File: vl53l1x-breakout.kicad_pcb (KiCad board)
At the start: 4 copper layers, 28 x 21.5 mm, 30 parts, among them J0 SM07B-SRSS-TBLFSN, J1 SM07B-SRSS-TBLFSN, U1 PCA9615DPJ, U2 VL53L1CXV0FY_1, U3 LTC4316IMSPBF

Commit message: cleanup routing a bit
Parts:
- moved C1 6.17 mm to (115.9, 132.3), turned to 0 degrees
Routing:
- net VCC: track 40.8 -> 53.0 mm, vias 9 -> 10
- net shld: track 32.3 -> 29.5 mm
- net GND: track 30.3 -> 31.4 mm
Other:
- board text added: "VL53L1X diff. breakout @kemfic 2022 rev. 0"
- board text removed: "VL53L1X Diff. Breakout @kemfic 2022 rev. 0"

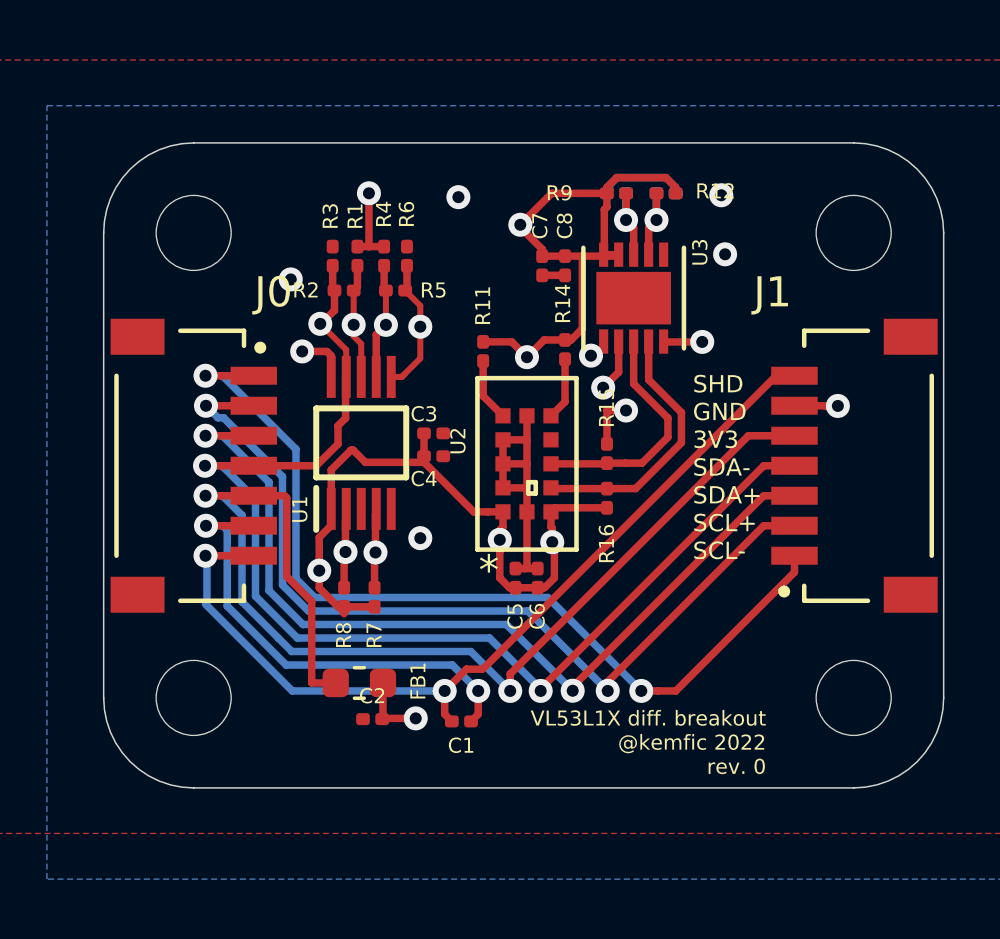
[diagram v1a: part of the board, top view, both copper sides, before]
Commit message: ordered but the pinout is flipped :/
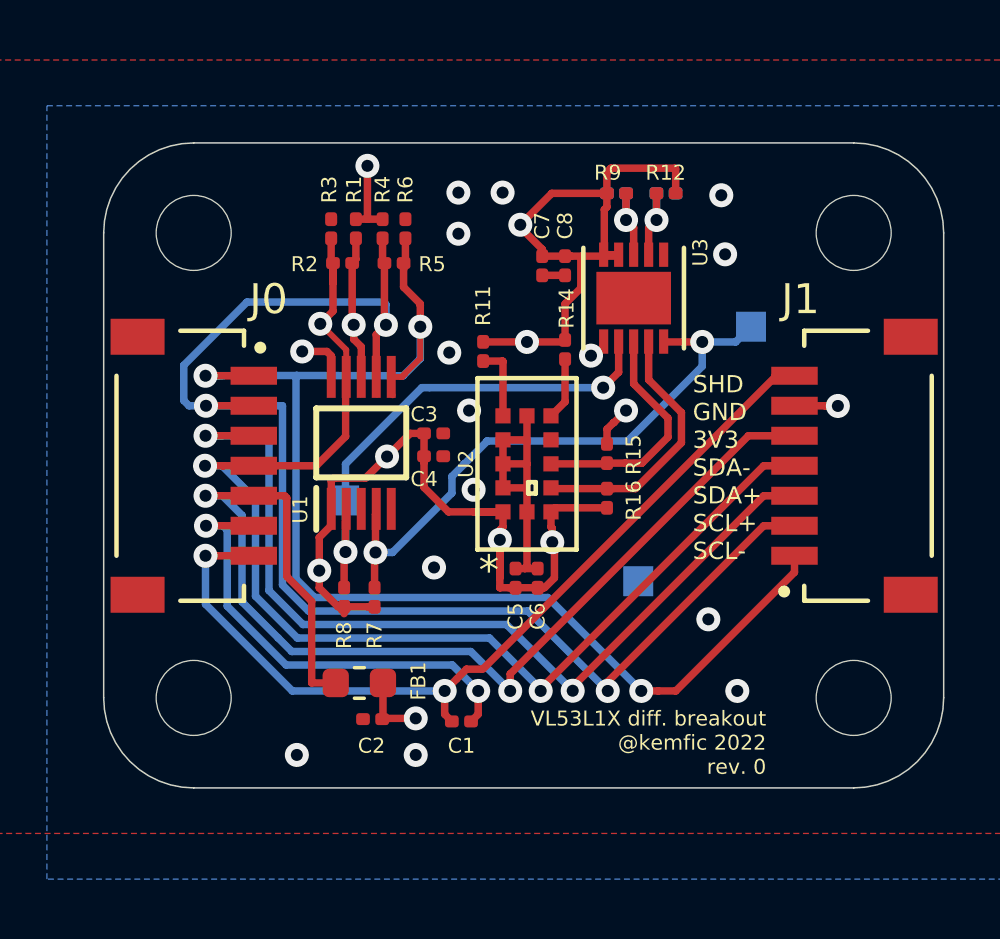
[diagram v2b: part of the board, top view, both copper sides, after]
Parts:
- added GND: TestPoint_Pad_1.0x1.0mm, TestPoint:TestPoint_Pad_1.0x1.0mm, B.Cu at (121.8, 127.6)
- added SCL: TestPoint_Pad_1.0x1.0mm, TestPoint:TestPoint_Pad_1.0x1.0mm, B.Cu at (125.6, 119.1)
- added SDA: TestPoint_Pad_1.0x1.0mm, TestPoint:TestPoint_Pad_1.0x1.0mm, B.Cu at (112.0, 124.9)
- moved R1 0.92 mm to (112.4, 115.9)
- moved R2 0.92 mm to (112.0, 117.0)
- moved R3 0.92 mm to (111.6, 115.9)
- moved R4 0.92 mm to (113.3, 115.9)
- moved R5 0.92 mm to (113.7, 117.0)
- moved R6 0.92 mm to (114.1, 115.9)
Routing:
- net SCL+: track 43.2 -> 48.7 mm
- net SDA+: track 43.0 -> 46.6 mm
- net GND: track 31.4 -> 28.6 mm, vias 8 -> 17
- net SCL: track 18.2 -> 20.4 mm
- net SDA-: track 40.5 -> 42.1 mm
- net VCC: track 53.0 -> 53.9 mm
- net SCL-: track 44.7 -> 45.3 mm

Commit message: [rev.1] fixed connector pinout
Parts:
- moved C2 17.7 mm to (111.6, 114.6), turned to 90 degrees
- moved FB1 16.1 mm to (110.4, 115.0), turned to 90 degrees
- moved C1 14.1 mm to (110.8, 119.1)
- moved R6 11.9 mm to (111.2, 127.4), turned to 270 degrees
- moved R3 11.9 mm to (114.4, 127.4), turned to 270 degrees
- moved R4 11.6 mm to (112.0, 127.4), turned to 90 degrees
- moved R1 11.6 mm to (113.6, 127.4), turned to 90 degrees
- moved R8 11.1 mm to (113.6, 117.1), turned to 270 degrees
- moved R7 11.0 mm to (112.6, 117.1), turned to 270 degrees
- moved R5 9.51 mm to (111.6, 126.3), turned to 180 degrees
- moved R2 9.50 mm to (114.0, 126.3), turned to 0 degrees
- moved SCL 9.32 mm to (117.3, 123.5)
- moved SDA 6.35 mm to (117.3, 121.5), turned to 180 degrees
- moved GND 4.47 mm to (117.3, 127.7)
- moved C3 1.00 mm to (115.5, 121.8)
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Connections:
- J0 pad 1: SCL- -> shld
- J0 pad 2: SCL+ -> GND
- J0 pad 3: SDA+ -> +3V3
- J0 pad 5: +3V3 -> SDA+
- J0 pad 6: GND -> SCL+
- J0 pad 7: shld -> SCL-
- J1 pad 1: SCL- -> shld
- J1 pad 2: SCL+ -> GND
- J1 pad 3: SDA+ -> +3V3
- J1 pad 5: +3V3 -> SDA+
- J1 pad 6: GND -> SCL+
- J1 pad 7: shld -> SCL-
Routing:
- net GND: track 28.6 -> 13.8 mm, vias 17 -> 10
- net SCL+: track 48.7 -> 38.1 mm, vias 3 -> 2
- net SCL-: track 45.3 -> 37.1 mm, vias 3 -> 1
- net SDA+: track 46.6 -> 38.4 mm, vias 3 -> 2
- net shld: track 29.5 -> 33.2 mm
- net VCC: track 53.9 -> 51.3 mm, vias 10 -> 9
- net SDA-: track 42.1 -> 39.9 mm, vias 3 -> 2
- net SDA: track 17.0 -> 15.3 mm
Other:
- board text added: "SCL- SCL+ SDA+ SDA- 3V3 GND SHD"
- board text added: "VL53L1X diff. breakout @kemfic 2022 rev. 1"
- board text removed: "SHD GND 3V3 SDA- SDA+ SCL+ SCL-"
- board text removed: "VL53L1X diff. breakout @kemfic 2022 rev. 0"

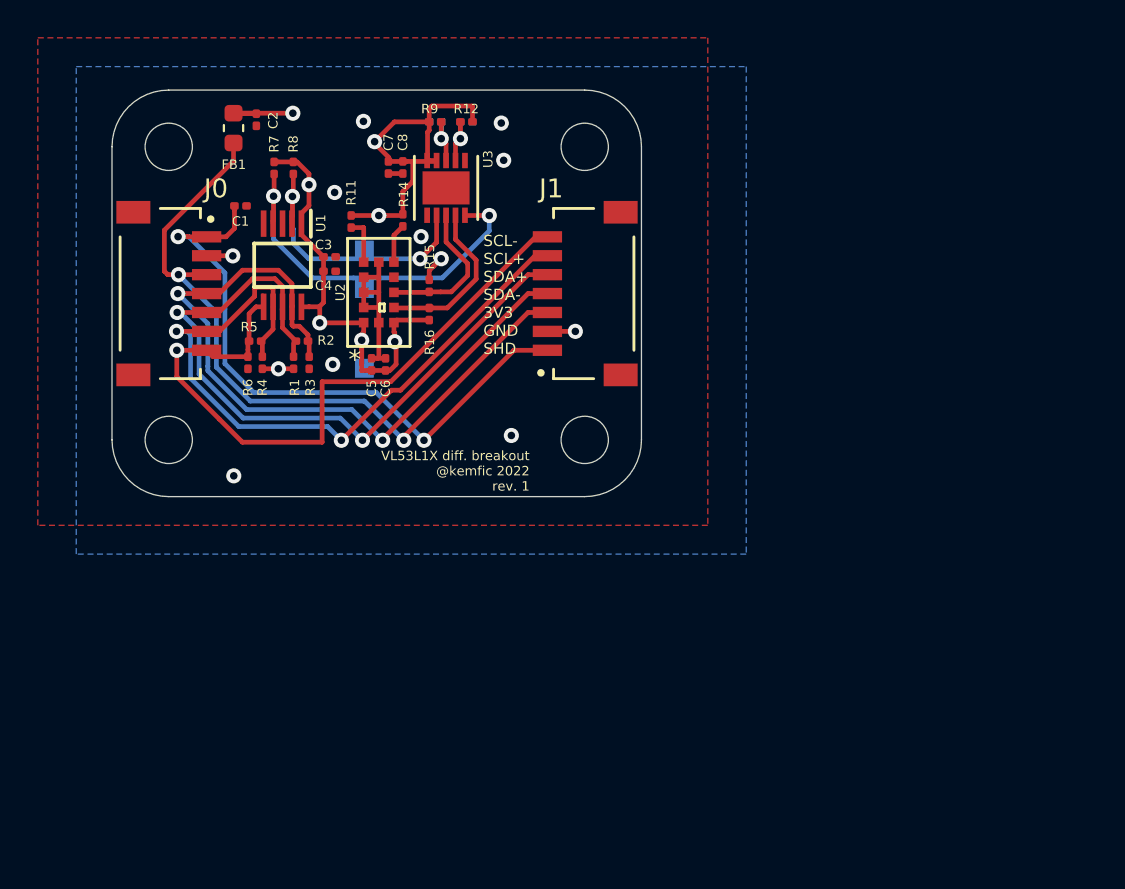
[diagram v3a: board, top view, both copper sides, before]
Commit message: using 0603s now
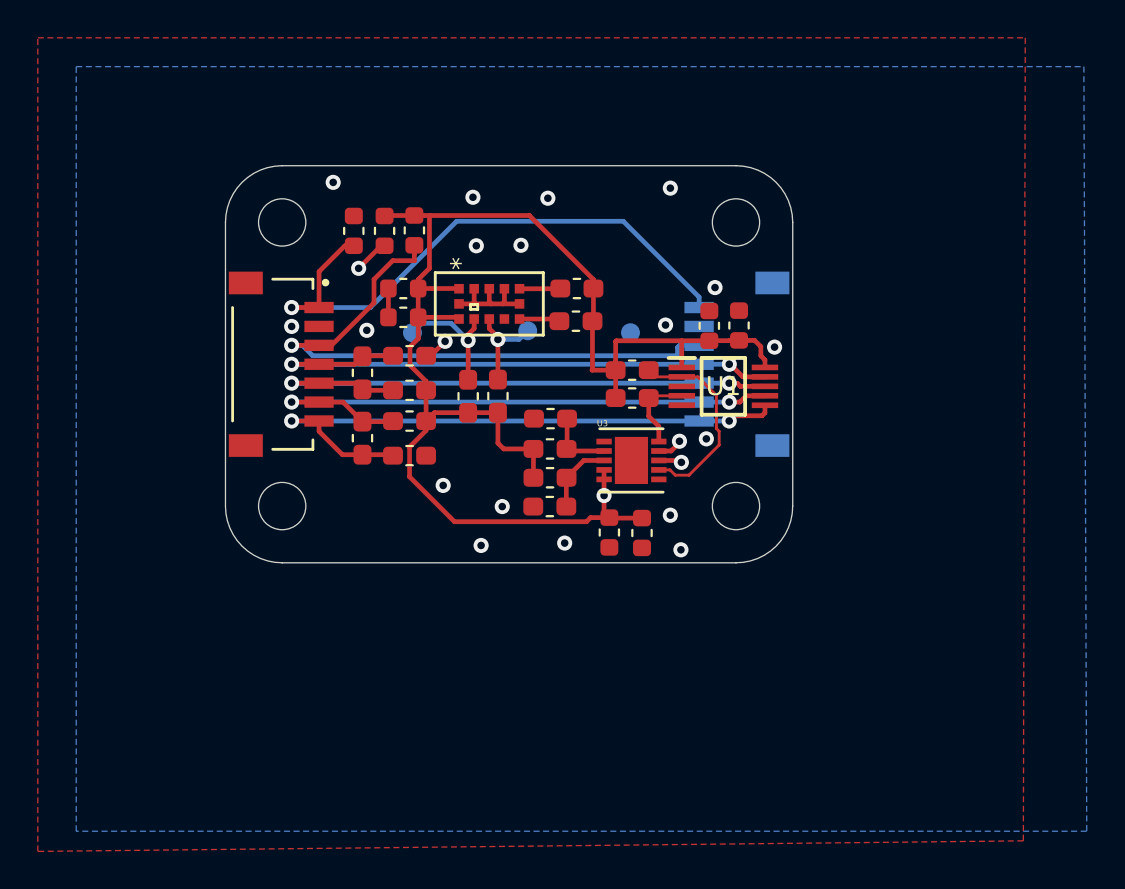
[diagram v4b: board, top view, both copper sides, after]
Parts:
- removed the GND at (117.3, 127.7)
- removed the SCL at (117.3, 123.5)
- removed the SDA at (117.3, 121.5)
- added GND: TestPoint_Pad_D1.0mm, TestPoint:TestPoint_Pad_D1.0mm, B.Cu at (131.4, 125.8)
- added REF**: MountingHole_2.5mm, MountingHole:MountingHole_2.5mm, F.Cu at (137.0, 135.0)
- added REF**: MountingHole_2.5mm, MountingHole:MountingHole_2.5mm, F.Cu at (113.0, 135.0)
- added REF**: MountingHole_2.5mm, MountingHole:MountingHole_2.5mm, F.Cu at (113.0, 120.0)
- added REF**: MountingHole_2.5mm, MountingHole:MountingHole_2.5mm, F.Cu at (137.0, 120.0)
- added SCL: TestPoint_Pad_D1.0mm, TestPoint:TestPoint_Pad_D1.0mm, B.Cu at (126.0, 125.7)
- added SDA: TestPoint_Pad_D1.0mm, TestPoint:TestPoint_Pad_D1.0mm, B.Cu at (119.9, 125.8)
- C1, C2, C3, C4, C5, C6, C7, C8: footprint Capacitor_SMD:C_0201_0603Metric -> Capacitor_SMD:C_0603_1608Metric
- J1: moved to B.Cu
- R1, R11, R12, R14, R15, R16, R2, R3, R4, R5, R6, R7, R8, R9: footprint Resistor_SMD:R_0201_0603Metric -> Resistor_SMD:R_0603_1608Metric_Pad1.05x0.95mm_HandSolder
- R10, R13: footprint Resistor_SMD:R_0201_0603Metric -> Resistor_SMD:R_0603_1608Metric_Pad1.05x0.95mm_HandSolder; moved to F.Cu
- U3: value LTC4316IMSPBF -> LTC4316IDD#PBF
- moved U1 24.2 mm to (136.3, 128.7), turned to 0 degrees
- moved C7 23.5 mm to (132.0, 136.4)
- moved R7 22.5 mm to (131.5, 129.3), turned to 0 degrees
- moved C8 22.2 mm to (130.3, 136.4)
- moved C3 22.0 mm to (137.2, 125.5), turned to 90 degrees
- moved R10 21.2 mm to (127.2, 135.0)
- moved R8 20.9 mm to (131.5, 127.8), turned to 0 degrees
- moved C4 20.3 mm to (135.6, 125.5), turned to 90 degrees
- moved R9 19.8 mm to (127.2, 133.5)
- moved R12 17.9 mm to (127.2, 132.0), turned to 0 degrees
- moved U3 17.4 mm to (131.5, 132.6), turned to 0 degrees
- moved R13 16.3 mm to (127.2, 130.4), turned to 180 degrees
- moved R11 12.5 mm to (128.6, 123.5), turned to 0 degrees
- moved FB1 11.0 mm to (120.0, 120.4)
- moved R14 10.6 mm to (128.5, 125.2), turned to 180 degrees
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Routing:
- net VCC: track 51.3 -> 78.5 mm, vias 9 -> 1
- net Net-(R16-Pad2): track 8.82 -> 25.3 mm, vias 0 -> 2
- net SCL: track 20.7 -> 4.32 mm, vias 2 -> 0
- net Net-(R15-Pad2): track 7.93 -> 20.5 mm, vias 0 -> 2
- net SDA-: track 39.9 -> 30.9 mm
- net SDA+: track 38.4 -> 30.9 mm
- net SCL+: track 38.1 -> 31.0 mm
- net +3V3: track 38.4 -> 32.6 mm, vias 2 -> 1
- net SCL-: track 37.1 -> 32.1 mm, vias 1 -> 2
- net SDA: track 15.3 -> 10.8 mm, vias 2 -> 0
- net GND: track 13.8 -> 10.4 mm, vias 10 -> 20
- net shld: track 33.2 -> 31.4 mm, vias 2 -> 1
- net Net-(R10-Pad1): track 3.04 -> 3.91 mm, vias 1 -> 0
- net Net-(R12-Pad2): track 3.04 -> 3.68 mm, vias 1 -> 0
- added copper zone on In1.Cu, net GND
- removed copper zone on In1.Cu, net VCC
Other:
- board size 28 x 21.5 mm -> 30 x 21 mm
- rule pad_to_mask_clearance: 0.051 -> 0.0508
- rule solder_mask_min_width: 0.25 -> 0.101
- board text removed: "SCL- SCL+ SDA+ SDA- 3V3 GND SHD"
- board text removed: "VL53L1X diff. breakout @kemfic 2022 rev. 1"
